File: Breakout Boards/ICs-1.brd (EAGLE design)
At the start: 170 x 95 mm, 51 parts

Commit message: breakout board update
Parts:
- added E$52, E$54: (no value), iStivi - LED:LED1210
- added E$53, E$55: (no value), iStivi - RCLD:R1206
- added E$56: (no value), iStivi - Header-Connector:1X04_LONGPADS
- moved E$49 12.0 mm to (36.4, 38.6)
- moved E$50 12.0 mm to (44.0, 34.8)
- moved E$51 12.0 mm to (28.8, 34.8)
- moved E$23 7.00 mm to (61.9, 38.6)
- moved E$25 7.00 mm to (54.2, 34.8)
- moved E$24 7.00 mm to (69.5, 34.8)
- moved E$11 4.00 mm to (86.8, 38.6)
- moved E$12 4.00 mm to (79.2, 34.8)
- moved E$4 4.00 mm to (94.4, 34.8)
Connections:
- new net S$205: E$52.A, E$53.1, E$56.1
- new net S$206: E$52.C, E$53.2, E$56.2
- new net S$207: E$54.A, E$55.1, E$56.3
- new net S$208: E$54.C, E$55.2, E$56.4
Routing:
- net S$205: track 0.00 -> 13.4 mm
- net S$208: track 0.00 -> 13.0 mm
- net S$207: track 0.00 -> 12.0 mm
- net S$206: track 0.00 -> 11.8 mm
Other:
- outline, holes or cut-outs redrawn

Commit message: boards update
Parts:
- moved E$53 2.49 mm to (7.20, 38.7), turned to 90 degrees
- moved E$55 2.46 mm to (19.9, 38.8), turned to 90 degrees
- moved E$54 0.80 mm to (17.5, 32.7)
- moved E$56 0.57 mm to (9.75, 44.2)
- moved E$52 0.57 mm to (9.51, 32.7)
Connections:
- new net S$209: E$54.C, E$55.1
- new net S$210: E$55.2, E$56.4
- net S$205: now also E$53.2; no longer E$52.A, E$53.1
- net S$206: now also E$52.A, E$53.1; no longer E$52.C, E$53.2, E$56.2
- net S$207: now also E$52.C, E$56.2; no longer E$54.A, E$55.1, E$56.3
- net S$208: now also E$54.A, E$56.3; no longer E$54.C, E$55.2, E$56.4
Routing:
- net S$205: track 13.4 -> 5.15 mm
- net S$206: track 11.8 -> 5.02 mm
- net S$209: track 0.00 -> 5.14 mm
- net S$210: track 0.00 -> 5.02 mm
- net S$208: track 13.0 -> 11.9 mm
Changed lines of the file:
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@@
 <setting verticaltext="up"/>
 </settings>
-<grid distance="0.05" unitdist="inch" unit="mm" style="lines" multiple="1" display="yes" altdistance="0.025" altunitdist="inch" altunit="inch"/>
+<grid distance="10" unitdist="mil" unit="mil" style="lines" multiple="1" display="yes" altdistance="0.025" altunitdist="inch" altunit="inch"/>
 <layers>
 <layer number="1" name="Top" color="4" fill="1" visible="yes" active="yes"/>
@@
 <circle x="28.764" y="39.878" radius="0.404" width="0.409" layer="116"/>
 <circle x="28.764" y="42.418" radius="0.404" width="0.409" layer="116"/>
-<circle x="10" y="43.73" radius="0.404" width="0.409" layer="116"/>
-<circle x="12.54" y="43.73" radius="0.404" width="0.409" layer="116"/>
-<circle x="15.08" y="43.73" radius="0.404" width="0.409" layer="116"/>
-<circle x="17.62" y="43.73" radius="0.404" width="0.409" layer="116"/>
+<circle x="9.746" y="44.238" radius="0.404" width="0.409" layer="116"/>
+<circle x="12.286" y="44.238" radius="0.404" width="0.409" layer="116"/>
+<circle x="14.826" y="44.238" radius="0.404" width="0.409" layer="116"/>
+<circle x="17.366" y="44.238" radius="0.404" width="0.409" layer="116"/>
 </plain>
 <attributes>
@@
 <element name="E$50" library="iStivi - Header-Connector" package="1X04_LONGPADS" value="" x="44.004" y="34.798" rot="R90"/>
 <element name="E$51" library="iStivi - Header-Connector" package="1X04_LONGPADS" value="" x="28.764" y="34.798" rot="R90"/>
-<element name="E$52" library="iStivi - LED" package="LED1210" value="" x="9" y="33"/>
-<element name="E$53" library="iStivi - RCLD" package="R1206" value="" x="9" y="37"/>
-<element name="E$54" library="iStivi - LED" package="LED1210" value="" x="18.27" y="33"/>
-<element name="E$55" library="iStivi - RCLD" package="R1206" value="" x="18.27" y="37"/>
-<element name="E$56" library="iStivi - Header-Connector" package="1X04_LONGPADS" value="" x="10" y="43.73"/>
+<element name="E$52" library="iStivi - LED" package="LED1210" value="" x="9.508" y="32.746"/>
+<element name="E$53" library="iStivi - RCLD" package="R1206" value="" x="7.196" y="38.718" rot="R90"/>
+<element name="E$54" library="iStivi - LED" package="LED1210" value="" x="17.508" y="32.746"/>
+<element name="E$55" library="iStivi - RCLD" package="R1206" value="" x="19.896" y="38.844" rot="R90"/>
+<element name="E$56" library="iStivi - Header-Connector" package="1X04_LONGPADS" value="" x="9.746" y="44.238"/>
 </elements>
 <signals>
@@
 </signal>
 <signal name="S$205">
+<contactref element="E$53" pad="2"/>
+<contactref element="E$56" pad="1"/>
+<wire x1="7.196" y1="40.14" x2="7.196" y2="41.486" width="1.016" layer="1"/>
+<wire x1="7.196" y1="41.486" x2="9.652" y2="43.942" width="1.016" layer="1"/>
+<wire x1="9.652" y1="43.942" x2="9.652" y2="44.144" width="1.016" layer="1"/>
+<wire x1="9.652" y1="44.144" x2="9.746" y2="44.238" width="1.016" layer="1"/>
+</signal>
+<signal name="S$206">
+<contactref element="E$52" pad="A"/>
 <contactref element="E$53" pad="1"/>
-<contactref element="E$56" pad="1"/>
-<wire x1="10" y1="43.73" x2="7.578" y2="43.73" width="1.016" layer="1"/>
-<wire x1="7.578" y1="43.73" x2="7.578" y2="37" width="1.016" layer="1"/>
-<contactref element="E$52" pad="A"/>
-<wire x1="7.578" y1="37" x2="7.62" y2="37" width="1.016" layer="1"/>
-<wire x1="7.62" y1="37" x2="7.62" y2="33.02" width="1.016" layer="1"/>
-<wire x1="7.62" y1="33.02" x2="7.4" y2="33.02" width="1.016" layer="1"/>
-<wire x1="7.4" y1="33.02" x2="7.4" y2="33" width="1.016" layer="1"/>
-</signal>
-<signal name="S$206">
-<contactref element="E$53" pad="2"/>
+<wire x1="7.908" y1="32.746" x2="7.112" y2="33.542" width="1.016" layer="1"/>
+<wire x1="7.112" y1="33.542" x2="7.112" y2="37.338" width="1.016" layer="1"/>
+<wire x1="7.112" y1="37.338" x2="7.154" y2="37.296" width="1.016" layer="1"/>
+<wire x1="7.154" y1="37.296" x2="7.196" y2="37.296" width="1.016" layer="1"/>
+</signal>
+<signal name="S$207">
 <contactref element="E$56" pad="2"/>
 <contactref element="E$52" pad="C"/>
-<wire x1="12.54" y1="43.73" x2="12.54" y2="39.118" width="1.016" layer="1"/>
-<wire x1="12.54" y1="39.118" x2="10.422" y2="37" width="1.016" layer="1"/>
-<wire x1="10.422" y1="37" x2="10.6" y2="37" width="1.016" layer="1"/>
-<wire x1="10.6" y1="37" x2="10.6" y2="33" width="1.016" layer="1"/>
-</signal>
-<signal name="S$207">
+<wire x1="11.108" y1="32.746" x2="12.286" y2="33.924" width="1.016" layer="1"/>
+<wire x1="12.286" y1="33.924" x2="12.286" y2="44.238" width="1.016" layer="1"/>
+</signal>
+<signal name="S$208">
+<contactref element="E$54" pad="A"/>
+<contactref element="E$56" pad="3"/>
+<wire x1="15.908" y1="32.746" x2="14.826" y2="33.828" width="1.016" layer="1"/>
+<wire x1="14.826" y1="33.828" x2="14.826" y2="44.238" width="1.016" layer="1"/>
+</signal>
+<signal name="S$209">
 <contactref element="E$55" pad="1"/>
-<contactref element="E$56" pad="3"/>
-<contactref element="E$54" pad="A"/>
-<wire x1="15.08" y1="43.73" x2="15.08" y2="38.768" width="1.016" layer="1"/>
-<wire x1="15.08" y1="38.768" x2="16.848" y2="37" width="1.016" layer="1"/>
-<wire x1="16.848" y1="37" x2="16.51" y2="37" width="1.016" layer="1"/>
-<wire x1="16.51" y1="37" x2="16.51" y2="33.02" width="1.016" layer="1"/>
-<wire x1="16.51" y1="33.02" x2="16.67" y2="33.02" width="1.016" layer="1"/>
-<wire x1="16.67" y1="33.02" x2="16.67" y2="33" width="1.016" layer="1"/>
-</signal>
-<signal name="S$208">
+<contactref element="E$54" pad="C"/>
+<wire x1="19.108" y1="32.746" x2="20.066" y2="33.704" width="1.016" layer="1"/>
+<wire x1="20.066" y1="33.704" x2="20.066" y2="37.084" width="1.016" layer="1"/>
+<wire x1="20.066" y1="37.084" x2="19.896" y2="37.254" width="1.016" layer="1"/>
+<wire x1="19.896" y1="37.254" x2="19.896" y2="37.422" width="1.016" layer="1"/>
+</signal>
+<signal name="S$210">
 <contactref element="E$55" pad="2"/>
 <contactref element="E$56" pad="4"/>
-<contactref element="E$54" pad="C"/>
-<wire x1="17.62" y1="43.73" x2="19.692" y2="43.73" width="1.016" layer="1"/>
-<wire x1="19.692" y1="43.73" x2="19.692" y2="37" width="1.016" layer="1"/>
-<wire x1="19.692" y1="37" x2="19.87" y2="37" width="1.016" layer="1"/>
-<wire x1="19.87" y1="37" x2="19.87" y2="33" width="1.016" layer="1"/>
+<wire x1="19.896" y1="40.266" x2="19.896" y2="41.708" width="1.016" layer="1"/>
+<wire x1="19.896" y1="41.708" x2="17.366" y2="44.238" width="1.016" layer="1"/>
 </signal>
 </signals>

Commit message: update cam job file
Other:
- board size 170 x 95 mm -> 150 x 75 mm
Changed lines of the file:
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@@
 <setting verticaltext="up"/>
 </settings>
-<grid distance="10" unitdist="mil" unit="mil" style="lines" multiple="1" display="yes" altdistance="0.025" altunitdist="inch" altunit="inch"/>
+<grid distance="10" unitdist="mil" unit="mm" style="lines" multiple="1" display="yes" altdistance="0.025" altunitdist="inch" altunit="inch"/>
 <layers>
 <layer number="1" name="Top" color="4" fill="1" visible="yes" active="yes"/>
@@
 <wire x1="24.7" y1="45.72" x2="24.7" y2="31.75" width="1" layer="46"/>
 <wire x1="24.7" y1="31.75" x2="47.56" y2="31.75" width="1" layer="46"/>
-<wire x1="0" y1="0" x2="-10" y2="0" width="0.3048" layer="20"/>
-<wire x1="-10" y1="0" x2="0" y2="-10" width="0.3048" layer="20"/>
-<wire x1="0" y1="-10" x2="0" y2="0" width="0.3048" layer="20"/>
-<wire x1="150" y1="0" x2="150" y2="-10" width="0.3048" layer="20"/>
-<wire x1="150" y1="-10" x2="160" y2="0" width="0.3048" layer="20"/>
-<wire x1="160" y1="0" x2="150" y2="0" width="0.3048" layer="20"/>
-<wire x1="150" y1="75" x2="150" y2="85" width="0.3048" layer="20"/>
-<wire x1="150" y1="85" x2="160" y2="75" width="0.3048" layer="20"/>
-<wire x1="160" y1="75" x2="150" y2="75" width="0.3048" layer="20"/>
-<wire x1="0" y1="75" x2="0" y2="85" width="0.3048" layer="20"/>
-<wire x1="0" y1="85" x2="-10" y2="75" width="0.3048" layer="20"/>
-<wire x1="-10" y1="75" x2="0" y2="75" width="0.3048" layer="20"/>
 <text x="37" y="79" size="1.778" layer="20">Breakout Boards</text>
 <text x="74" y="79" size="1.778" layer="1">TOP SOLDER</text>

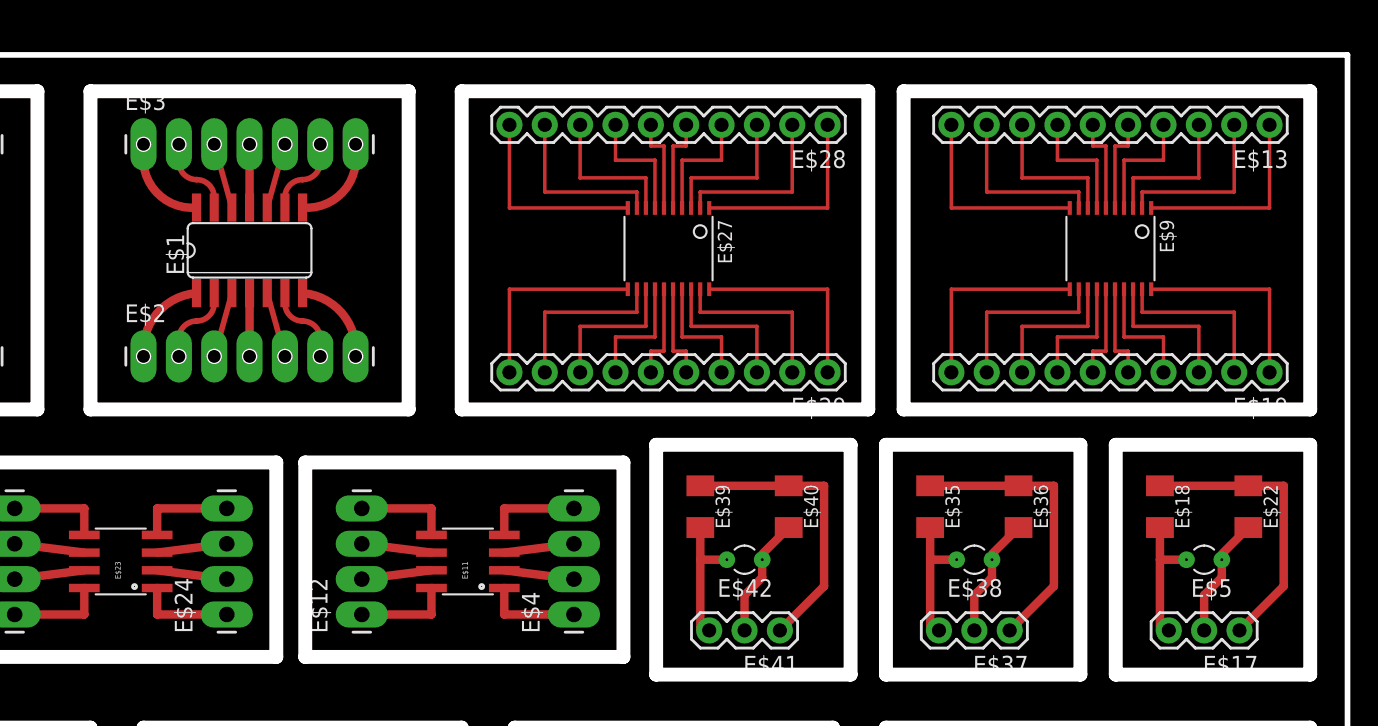
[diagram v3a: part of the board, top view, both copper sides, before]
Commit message: new ic breakout
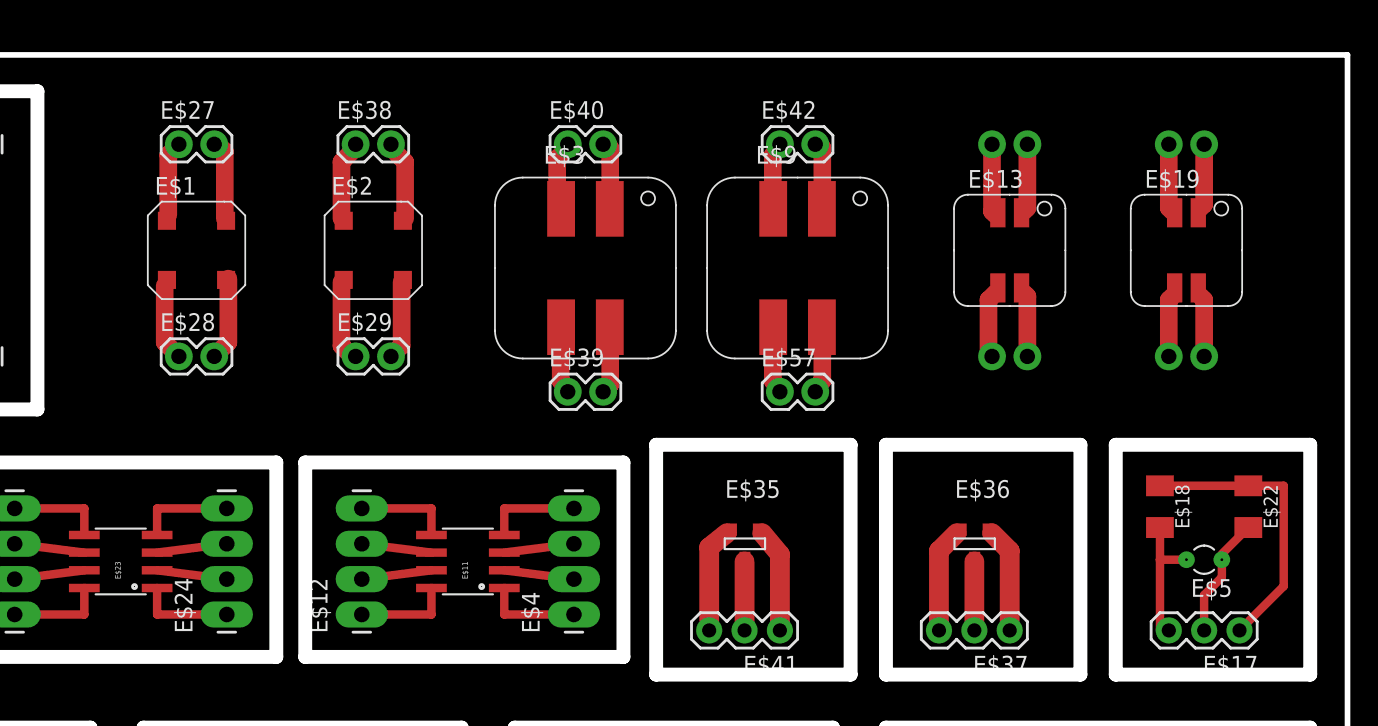
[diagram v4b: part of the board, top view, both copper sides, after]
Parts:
- added E$57, E$58, E$59, E$60, E$61: (no value), iStivi - Header-Connector:1X02
- E$1: device iStivi - ICs:SO14 -> iStivi - RCLD:LPR6235
- E$13, E$19: device iStivi - Header-Connector:1X10 -> iStivi - RCLD:MSD7342
- E$2: device iStivi - Header-Connector:1X07_LONGPADS -> iStivi - RCLD:LPR6235
- E$27: device iStivi - ICs:TSSOP20 -> iStivi - Header-Connector:1X02
- E$28, E$29: device iStivi - Header-Connector:1X10 -> iStivi - Header-Connector:1X02
- E$3: device iStivi - Header-Connector:1X07_LONGPADS -> iStivi - RCLD:MSD1260
- E$35, E$36: device iStivi - RCLD:C1206K -> iStivi - Transistor-FET-reg:SOT-23
- E$38, E$42: device iStivi - Oscillators:TC26V -> iStivi - Header-Connector:1X02
- E$39, E$40: device iStivi - RCLD:C1206K -> iStivi - Header-Connector:1X02
- E$9: device iStivi - ICs:TSSOP20 -> iStivi - RCLD:MSD1260
- moved E$38 53.5 mm to (78.7, 68.6), turned to 0 degrees
- moved E$28 49.5 mm to (66.0, 53.3), turned to 0 degrees
- moved E$27 36.0 mm to (66.0, 68.6), turned to 0 degrees
- moved E$29 33.9 mm to (78.7, 53.3), turned to 0 degrees
- moved E$3 33.0 mm to (95.2, 59.7)
- moved E$40 30.5 mm to (94.0, 68.6), turned to 0 degrees
- moved E$42 30.0 mm to (109.2, 68.6), turned to 0 degrees
- moved E$9 22.5 mm to (110.5, 59.7), turned to 0 degrees
- moved E$13 20.7 mm to (125.7, 61.0), turned to 0 degrees
- moved E$2 18.2 mm to (80.0, 61.0)
- moved E$35 13.6 mm to (106.7, 39.9), turned to 0 degrees
- moved E$39 12.6 mm to (94.0, 50.8), turned to 0 degrees
- moved E$19 10.6 mm to (138.4, 61.0), turned to 0 degrees
- moved E$36 4.15 mm to (123.2, 39.9), turned to 0 degrees
- moved E$1 3.81 mm to (67.3, 61.0)
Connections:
- removed net S$10: E$1.12, E$3.3
- removed net S$107: E$27.9, E$28.9
- removed net S$11: E$1.11, E$3.4
- removed net S$112: E$27.10, E$28.10
- removed net S$113: E$27.20, E$29.1
- removed net S$114: E$27.19, E$29.2
- removed net S$115: E$27.18, E$29.3
- removed net S$116: E$27.17, E$29.4
- removed net S$117: E$27.16, E$29.5
- removed net S$118: E$27.15, E$29.6
- removed net S$119: E$27.14, E$29.7
- removed net S$120: E$27.12, E$29.9
- removed net S$121: E$27.13, E$29.8
- removed net S$122: E$27.11, E$29.10
- removed net S$13: E$1.9, E$3.6
- removed net S$14: E$1.8, E$3.7
- removed net S$151: E$35.2, E$37.3
- removed net S$152: E$36.2, E$37.2
- removed net S$153: E$35.1, E$36.1, E$37.1
- removed net S$156: E$39.1, E$40.1, E$41.1
- removed net S$4: E$1.4, E$2.4
- removed net S$41: E$27.1, E$28.1
- removed net S$42: E$27.2, E$28.2
- removed net S$43: E$27.3, E$28.3
- removed net S$44: E$27.4, E$28.4
- removed net S$5: E$1.5, E$2.5
- removed net S$6: E$1.6, E$2.6
- removed net S$7: E$1.7, E$2.7
- removed net S$73: E$13.3, E$9.3
- removed net S$74: E$13.4, E$9.4
- removed net S$75: E$13.5, E$9.5
- removed net S$76: E$13.6, E$9.6
- removed net S$77: E$13.7, E$9.7
- removed net S$78: E$13.8, E$9.8
- removed net S$79: E$13.9, E$9.9
- removed net S$8: E$1.14, E$3.1
- removed net S$80: E$13.10, E$9.10
- removed net S$81: E$19.1, E$9.20
- removed net S$82: E$19.2, E$9.19
- removed net S$83: E$19.3, E$9.18
- removed net S$84: E$19.4, E$9.17
- removed net S$85: E$19.5, E$9.16
- removed net S$86: E$19.6, E$9.15
- removed net S$87: E$19.7, E$9.14
- removed net S$88: E$19.9, E$9.12
- removed net S$89: E$19.8, E$9.13
- removed net S$9: E$1.13, E$3.2
- removed net S$90: E$19.10, E$9.11
- net S$1: now also E$28.1; no longer E$1.1, E$2.1
- net S$12: now also E$39.2; no longer E$1.10, E$3.5
- net S$154: no longer E$39.2
- net S$155: now also E$37.3; no longer E$40.2, E$41.2
- net S$2: now also E$28.2; no longer E$1.2, E$2.2
- net S$3: now also E$27.1; no longer E$1.3, E$2.3
- net S$45: now also E$59.2; no longer E$27.5, E$28.5
- net S$46: now also E$59.1; no longer E$27.6, E$28.6
- net S$47: now also E$61.2; no longer E$27.7, E$28.7
- net S$48: now also E$61.1; no longer E$27.8, E$28.8
- net S$71: now also E$60.2; no longer E$13.1, E$9.1
- net S$72: now also E$60.1; no longer E$13.2, E$9.2
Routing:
- net S$156: track 20.6 -> 5.08 mm
- net S$153: track 20.6 -> 5.08 mm
- net S$80: track 14.5 -> 0.00 mm
- net S$90: track 14.5 -> 0.00 mm
- net S$112: track 14.5 -> 0.00 mm
- net S$81: track 14.5 -> 0.00 mm
- net S$122: track 14.5 -> 0.00 mm
- net S$113: track 14.5 -> 0.00 mm
- net S$107: track 12.6 -> 0.00 mm
- net S$82: track 12.6 -> 0.00 mm
- net S$120: track 12.6 -> 0.00 mm
- net S$79: track 12.6 -> 0.00 mm
- net S$88: track 12.6 -> 0.00 mm
- net S$114: track 12.6 -> 0.00 mm
- net S$115: track 10.7 -> 0.00 mm
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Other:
- outline, holes or cut-outs redrawn
